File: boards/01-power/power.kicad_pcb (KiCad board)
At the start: 8 copper layers, 61.2 x 50 mm, 46 parts, among them J1 CONN_DF40_100P_F, J2 USB_C_Receptacle_USB2.0_16P, J3 TC2030, J4 TC2030, P1 MAG_RB1_125BAG1A, SW1 SW_BOOT, SW2 SW_BOOT, U1 USBLC6-2P6, U2 AP63203WU, U3 STM32F405RGTx, U4 PMIC_TPS2372_4RGWR, Y1 16Mhz

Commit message: feat: pogo pins
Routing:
- net unconnected-(J5-SWDIO-Pad2): track 0.00 -> 22.0 mm
- net unconnected-(J5-GND-Pad5): track 0.00 -> 15.0 mm, vias 0 -> 1
- net unconnected-(J5-~{RESET}-Pad3): track 0.00 -> 14.0 mm
- net unconnected-(J5-SWCLK-Pad4): track 0.00 -> 14.0 mm
- net unconnected-(J5-SWO-Pad6): track 0.00 -> 13.6 mm, vias 0 -> 1
- net unconnected-(J5-VCC-Pad1): track 8.05 -> 15.7 mm, vias 0 -> 6
- net (no net): vias 14 -> 10

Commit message: fix: align jtag probe reference
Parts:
- renumbered JTAG to J5
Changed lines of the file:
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@@
 		(descr "Generated from CONN_TC2030_JTAG.kicad_mod; TC2030 pitch 1.27 mm, C5157236 tip 0.80 mm leaves 0.47 mm between tips, barrel 1.20 mm leaves 0.07 mm between barrels")
 		(tags "tc2030 jtag swd pogo probe card-edge")
-		(property "Reference" "JTAG"
+		(property "Reference" "J5"
 			(at 0 6.875 0)
 			(layer "F.SilkS")
@@
 		)
 		(embedded_fonts no)
-		(model "/home/pixel/dev/woki-cam/lib/cad/CONN_TC2030_JTAG_PROBE.step"
+		(model "${KIPRJMOD}/../../lib/cad/CONN_TC2030_JTAG_PROBE.step"
 			(offset
 				(xyz 0 -0.65 0)

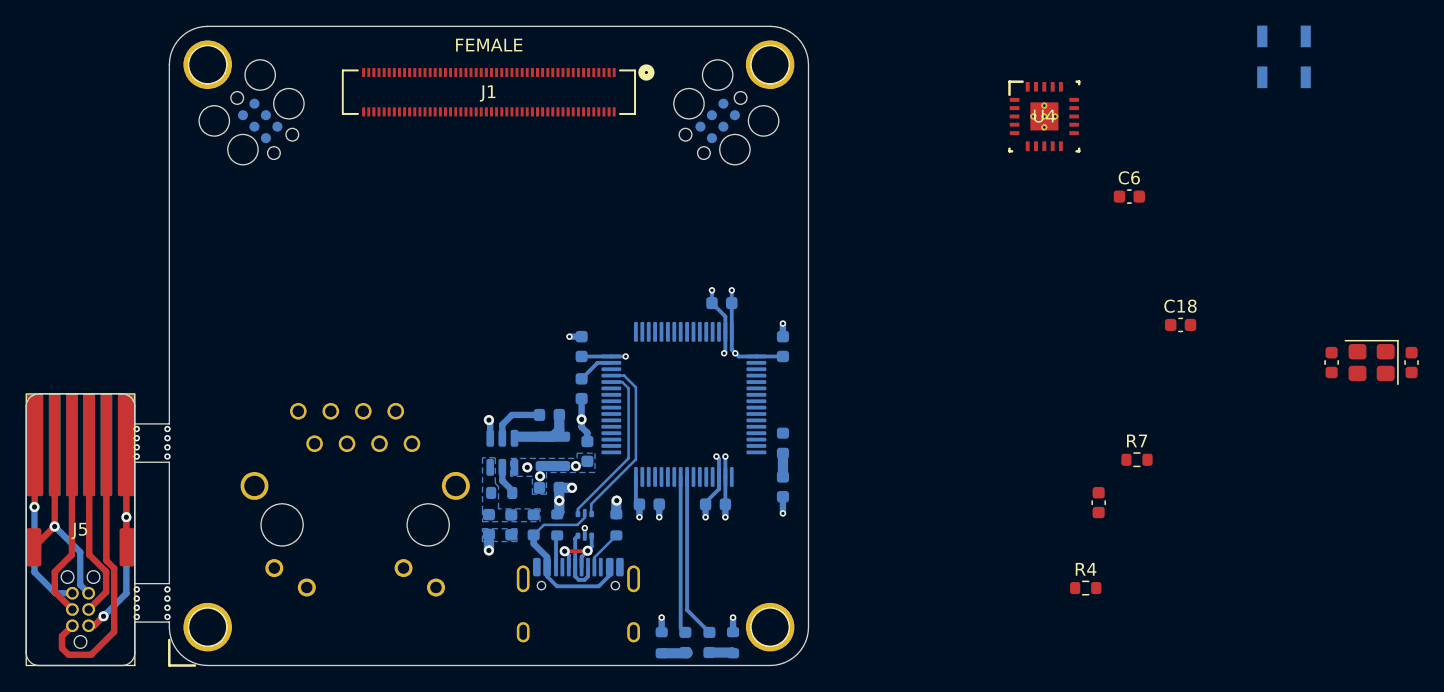
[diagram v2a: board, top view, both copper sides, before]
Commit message: finish: stm32/added icons
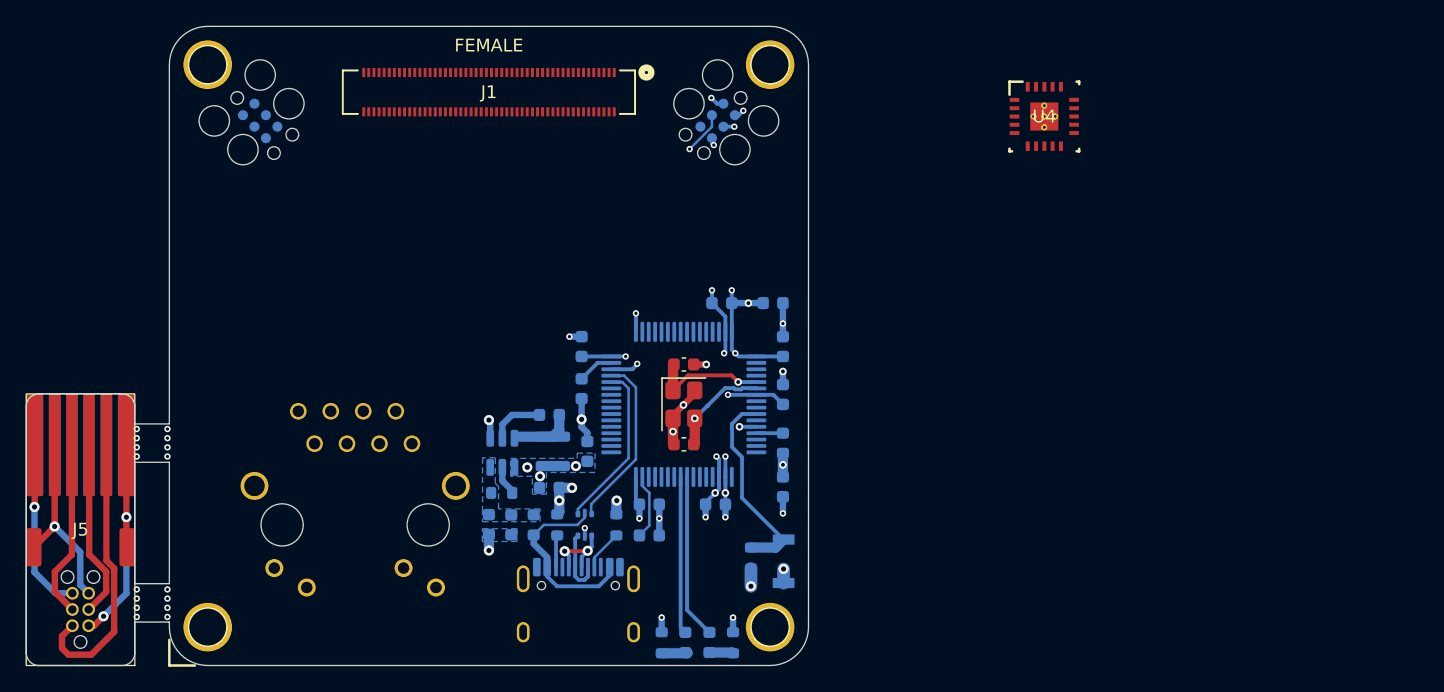
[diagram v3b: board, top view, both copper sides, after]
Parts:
- removed R4: 10k, Resistor_SMD:R_0603_1608Metric
- removed SW1: SW_BOOT, Woki:SW_B3U_1000P
- C18, C6, C7, R7: moved to B.Cu
- moved C16 56.9 mm to (90.2, 76.5), turned to 0 degrees
- moved SW2 56.7 mm to (98.0, 91.8), turned to -90 degrees
- moved Y1 53.9 mm to (90.2, 79.6), turned to -90 degrees
- moved C17 51.1 mm to (90.2, 82.7), turned to 180 degrees
- moved C7 35.2 mm to (87.5, 89.8), turned to 0 degrees
- moved C18 31.6 mm to (98.0, 78.8), turned to 90 degrees
- moved R7 31.2 mm to (95.5, 91.6), turned to -90 degrees
- moved C6 29.1 mm to (97.2, 71.7)
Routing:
- net /STM32/~{STM_RESET}: track 0.00 -> 33.1 mm, vias 0 -> 2
- net /STM32/SYS_JTMS-SWDIO: track 0.00 -> 31.1 mm, vias 0 -> 2
- net /STM32/SYS_JTCK-SWCLK: track 0.00 -> 19.4 mm, vias 0 -> 2
- net /STM32/USR_BTN1: track 0.00 -> 15.8 mm
- net GND: track 28.0 -> 41.3 mm, vias 17 -> 25
- net Net-(U3-PH0): track 0.00 -> 9.36 mm, vias 0 -> 1
- net Net-(U3-PH1): track 0.00 -> 7.96 mm, vias 0 -> 1
- net Net-(U3-VCAP_1): track 0.00 -> 5.12 mm
- net +3.3V: track 22.6 -> 27.1 mm, vias 9 -> 14
- net Net-(U3-VDDA): track 0.00 -> 2.08 mm

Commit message: poe: class 8 negotiate(max around 62W-71W at PD)
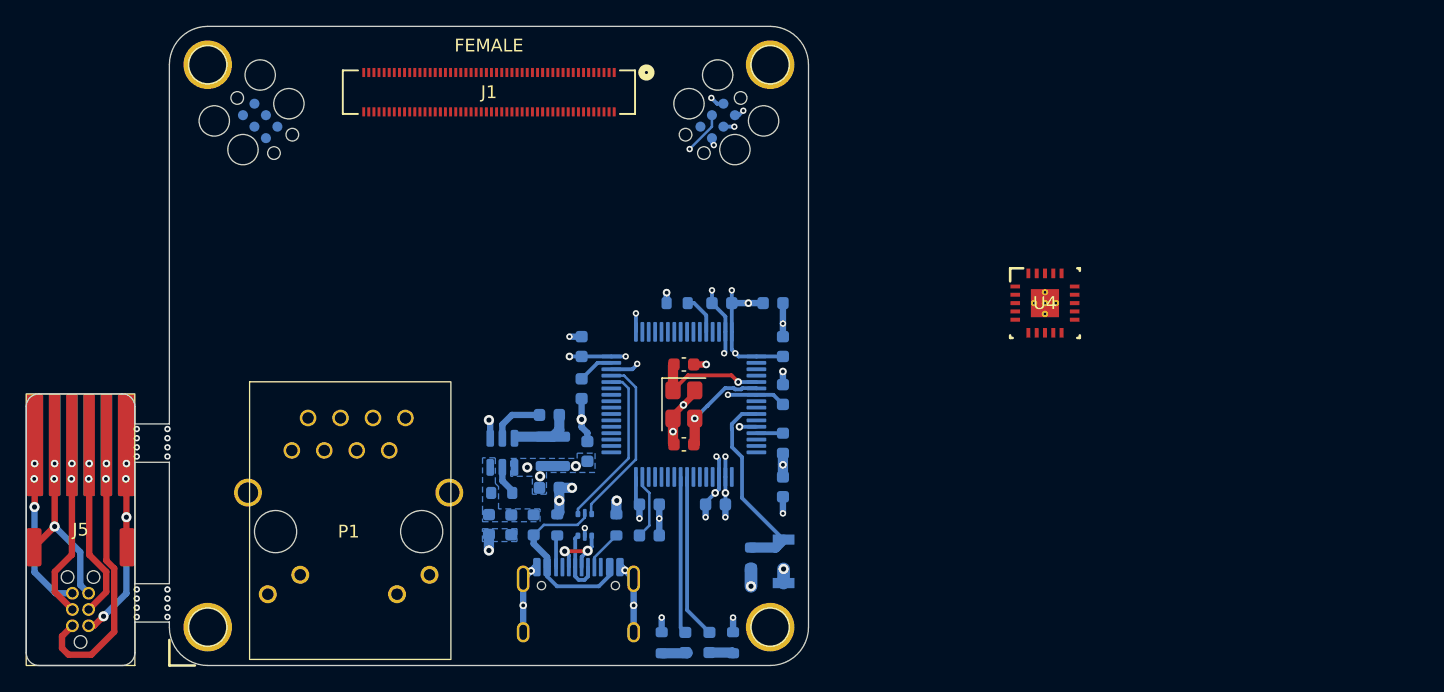
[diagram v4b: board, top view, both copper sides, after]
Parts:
- added R8: 10k, Resistor_SMD:R_0603_1608Metric, B.Cu at (89.7, 71.7)
- P1: moved to F.Cu
- moved U4 14.6 mm to (118.5, 71.7)
- moved P1 0.73 mm to (64.0, 89.5), turned to 0 degrees
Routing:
- net GND: track 41.3 -> 53.5 mm, vias 25 -> 30
- net /STM32/~{STM_RESET}: track 33.1 -> 29.7 mm
- net /STM32/BOOT0: track 0.00 -> 3.14 mm
- net +3.3V: track 27.1 -> 28.0 mm, vias 14 -> 15
- net unconnected-(J5-~{RESET}-Pad3): vias 0 -> 2
- net unconnected-(J5-VCC-Pad1): vias 6 -> 8
- net unconnected-(J5-SWO-Pad6): vias 1 -> 3
- net unconnected-(J5-SWDIO-Pad2): vias 0 -> 2
- net unconnected-(J5-SWCLK-Pad4): vias 0 -> 2
- net unconnected-(J5-GND-Pad5): vias 1 -> 3

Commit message: poe: magjack
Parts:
- added C19: 100u, Capacitor_SMD:CP_Elec_8x10, F.Cu at (126.1, 67.7)
- added C9: 100n, Capacitor_SMD:C_0603_1608Metric, F.Cu at (118.0, 64.0)
- added D3: LED, LED_SMD:LED_0603_1608Metric, F.Cu at (128.7, 73.9)
- added D4: LED, LED_SMD:LED_0603_1608Metric, F.Cu at (128.7, 76.5)
- added R10: 63.4R, Resistor_SMD:R_0603_1608Metric, F.Cu at (118.0, 69.0)
- added R11: 90.9R, Resistor_SMD:R_0603_1608Metric, F.Cu at (118.0, 71.5)
- added R12: 49.9k, Resistor_SMD:R_0603_1608Metric, F.Cu at (118.0, 74.0)
- added R13: 1.3k, Resistor_SMD:R_0805_2012Metric, F.Cu at (128.9, 79.3)
- added R14: 100k, Resistor_SMD:R_0603_1608Metric, F.Cu at (118.0, 76.6)
- added R15: 100k, Resistor_SMD:R_0603_1608Metric, F.Cu at (118.0, 79.1)
- added R16: 49.9k, Resistor_SMD:R_0603_1608Metric, F.Cu at (118.0, 81.6)
- added R9: 24.9k, Resistor_SMD:R_0603_1608Metric, F.Cu at (118.0, 66.5)
- P1: moved to B.Cu
- moved U4 6.45 mm to (123.3, 75.9)
- moved P1 0.15 mm to (64.2, 89.5), turned to 180 degrees
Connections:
- P1 pad S1: (no net) -> unconnected-(P1-SHIELD-PadS1)
- P1 pad S2: (no net) -> unconnected-(P1-SHIELD-PadS2)
- U4 pad 1: unconnected-(U4-VDD-Pad1) -> /POE/POE_VDD
- U4 pad 10: unconnected-(U4-AUTCLS_N-Pad10) -> /POE/POE_VSS
- U4 pad 11: unconnected-(U4-RTN-Pad11) -> /POE/POE_RTN
- U4 pad 12: unconnected-(U4-RTN-Pad12) -> /POE/POE_RTN
- U4 pad 13: unconnected-(U4-PG-Pad13) -> Net-(U4-PG)
- U4 pad 17: unconnected-(U4-TPL-Pad17) -> /POE/TPL
- U4 pad 18: unconnected-(U4-TPH-Pad18) -> /POE/TPH
- U4 pad 2: unconnected-(U4-DEN-Pad2) -> Net-(U4-DEN)
- U4 pad 21: unconnected-(U4-VSS-Pad21) -> /POE/POE_VSS
- U4 pad 3: unconnected-(U4-CLSA-Pad3) -> Net-(U4-CLSA)
- U4 pad 4: unconnected-(U4-VSS-Pad4) -> /POE/POE_VSS
- U4 pad 5: unconnected-(U4-VSS-Pad5) -> /POE/POE_VSS
- U4 pad 6: unconnected-(U4-CLSB-Pad6) -> Net-(U4-CLSB)
- U4 pad 7: unconnected-(U4-REF-Pad7) -> Net-(U4-REF)
- U4 pad 8: unconnected-(U4-AMPS_CTL-Pad8) -> Net-(U4-AMPS_CTL)
- U4 pad 9: unconnected-(U4-MPS_DUTY-Pad9) -> /POE/POE_VSS
